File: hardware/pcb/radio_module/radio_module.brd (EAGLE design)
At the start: 30 x 25 mm, 29 parts, among them T1 DDTC114, T2 DDTC114, U1 MAX2769LPKF, X1 SMA

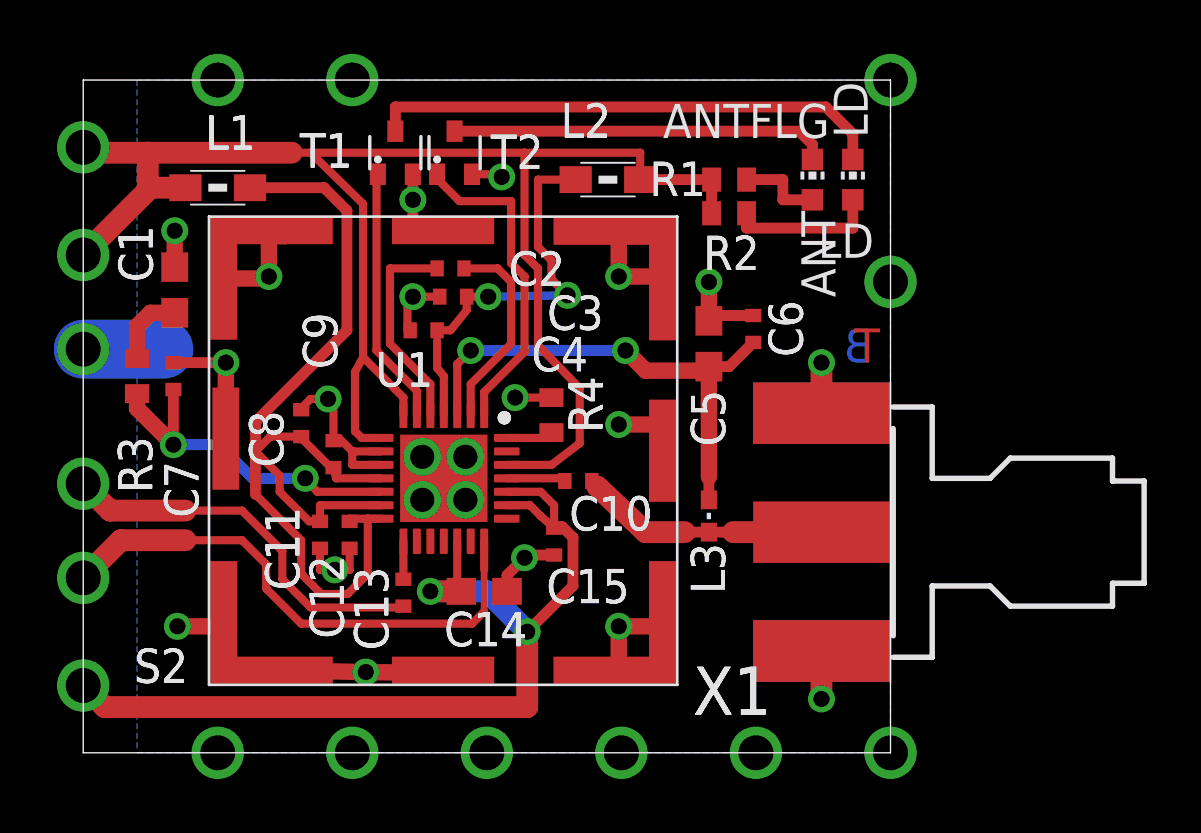
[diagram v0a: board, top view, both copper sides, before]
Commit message: tidyup. removed outdated schematics. added latest version pcb/schematics
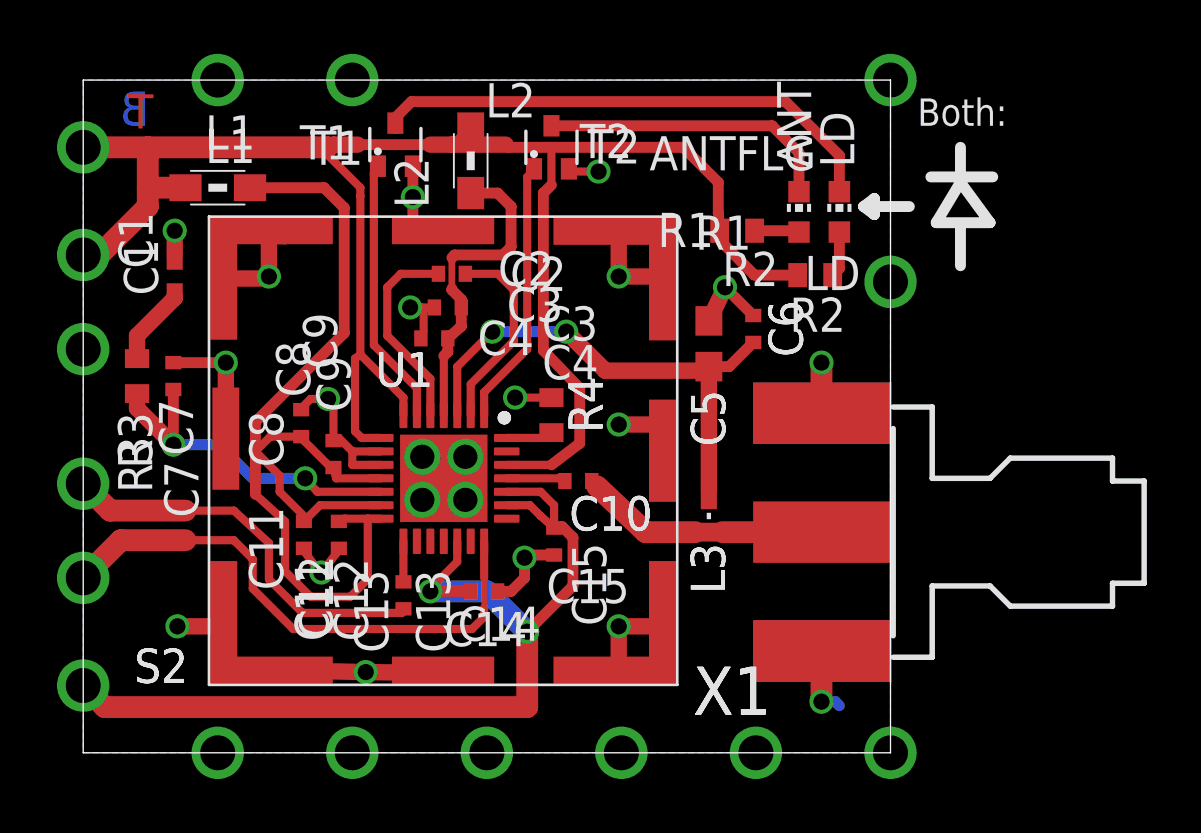
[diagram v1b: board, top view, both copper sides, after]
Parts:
- C1, C14: device rcl_1:C0603 -> rcl_1:C0402
- moved L2 5.15 mm to (14.4, 22.0), turned to 90 degrees
- moved R2 3.94 mm to (27.2, 17.8)
- moved T2 3.61 mm to (17.4, 22.5)
- moved R1 1.92 mm to (24.3, 19.4)
- moved ANTFLG 1.30 mm to (26.6, 20.1)
- moved LD 1.30 mm to (28.1, 20.1)
- moved C11 0.60 mm to (8.20, 8.10)
- moved C1 0.50 mm to (3.40, 17.7)
- moved C4 0.50 mm to (13.1, 15.4)
- moved C3 0.45 mm to (13.6, 16.6)
- moved C12 0.40 mm to (9.50, 8.10)
- moved T1 0.30 mm to (11.6, 22.6)
- moved C2 0.21 mm to (13.7, 17.8)
- moved C13 0.10 mm to (11.9, 5.85)
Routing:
- net VCC/2: track 98.6 -> 105.8 mm
- net N$16: track 5.55 -> 1.70 mm
- net +UB: track 15.1 -> 12.1 mm, vias 2 -> 0
- net N$8: track 14.1 -> 11.1 mm
- net ANTFLG: track 12.0 -> 9.93 mm
- net N$7: track 3.20 -> 1.67 mm
- net GNDA: track 64.5 -> 63.0 mm
- net V+: track 38.9 -> 39.5 mm
- net N$5: track 18.8 -> 19.4 mm
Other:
- board text added: "(c) 2014"
- board text added: "Both:"
- board text added: "Radio_board V1.00"
